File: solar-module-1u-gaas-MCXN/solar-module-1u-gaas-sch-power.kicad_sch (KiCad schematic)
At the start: 53 parts, among them Q1 NTR4101P, Q2 DMP2240UDM-7, U10 TPS63060DSCR, U12 LTC4412, U3 LT1618EMSTRPBF, U4 INA226

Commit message: Now solar module v1.2.
Upgraded CAN transciever to the 337, added version bits, removed silkscreen on cell outlines, double checked fastener heads, cleaned up documentation a lot, fixed ERCs and DRCs.
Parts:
- C12: DIS DIgiKey -> DigiKey; DPN 490-GRT21BC71E106KE13LCT-ND -> 490-GRT21BC71E106KE13KCT-ND; MPN GRT21BC71E106KE13L -> GRT21BC71E106KE13K
- C13, C20, C4: footprint oresat-passives:0603-C-NOSILK -> oresat-passives:0805-C-NOSILK; DIS DIgiKey -> DigiKey; DPN 490-12317-1-ND -> 490-GRT21BC71E106KE13KCT-ND; MPN GRT188R61C106KE13D -> GRT21BC71E106KE13K
- C15, C19, C23: footprint oresat-passives:0805-C-NOSILK -> oresat-passives:1206-C; DPN 490-9959-1-ND -> 490-12409-1-ND; MPN GRM21BR61E226ME44L -> GRT31CC81C226KE01L
- C18: DPN 587-4332-1-ND -> 490-GRT188C71C475KE13DCT-ND; MFR Taiyo Yuden -> Murata Electronics; MPN EMK107BBJ475KAHT -> GRT188C71C475KE13D
- C2: DIS DIgiKey -> DigiKey; DPN 399-14102-1-ND -> 399-12983-1-ND; MPN C0603C103J3GECAUTO -> C0603C103J5RACAUTO
- C21, C37, C6, C7, C8: DPN 587-3472-1-ND -> 399-6856-1-ND; MFR Taiyo Yuden -> KEMET; MPN TMK107BJ104KAHT -> C0603C104K5RACAUTO
- C22: DIS DIgiKey -> DigiKey; DPN 399-6840-1-ND -> 399-16015-1-ND; MPN C0603C100J5GACAUTO -> C0603C100J1GACAUTO
- Q1: DIS DIgiKey -> DigiKey; MFR On Semiconductor -> ON Semi
- Q2: DIS DIgiKey -> DigiKey
- U4: footprint Package_SO:VSSOP-10_3x3mm_P0.5mm -> Package_SO:TSSOP-10_3x3mm_P0.5mm
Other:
- moved on the sheet: C7

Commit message: Fixed Makefile to produce usable BOM. Updated BOM to correct DPNs, updated EOL'd components
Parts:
- D1, D3, L2, R18, R19, R2, R36, R37, R6, R7: DIS DIgiKey -> DigiKey
- D5: DIS DIgiKey -> DigiKey; DPN NRVB130LSFT1GOSTR-ND -> NRVB130LSFT1GOSCT-ND
- L1: DIS DIgiKey -> DigiKey; DPN 490-14160-2-ND -> 490-14160-1-ND
- Q1: DPN NTR4101PT1GOSCT-ND -> 31-DMP2035UQ-7CT-ND; MFR ON Semi -> Diodes Incorporated; MPN NTR4101PT1G -> DMP2035UQ-7
- R1: DIS DIgiKey -> DigiKey; DPN RMCF0603FT560KTR-ND -> RMCF0603FT560KCT-ND
- R10: DPN RMCF0603FT82K5TR-ND -> RMCF0603FT82K5CT-ND
- R12: DPN RMCF0603FT14K7TR-ND -> RMCF0603FT14K7CT-ND
- R16: DPN RMCF0603FT2K00TR-ND -> RMCF0603FT2K00CT-ND
- U10: DIS DIgiKey -> DigiKey; DPN 296-30204-2-ND -> 296-30204-1-ND
- U12: DIS DIgiKey -> DigiKey; DPN 505-LTC4412ES6#TRPBFTR-ND -> 505-LTC4412ES6#TRPBFCT-ND
- U3: DIS DIgiKey -> DigiKey; DPN LT1618EMS#TRPBFTR-ND -> LT1618EMS#TRPBFCT-ND
- U4: DIS DIgiKey -> DigiKey; DPN 296-29100-2-ND -> 296-29100-1-ND
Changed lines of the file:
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@@
 			)
 		)
-		(property "Datasheet" "https://www.onsemi.com/pdf/datasheet/ntr4101p-d.pdf"
+		(property "Datasheet" "https://www.diodes.com/assets/Datasheets/DMP2035U.pdf"
 			(at 307.34 95.25 0)
 			(hide yes)
@@
 			)
 		)
-		(property "Description" "P-Channel 20V 1.8A (Ta) 420mW (Ta) Surface Mount SOT-23-3 (TO-236)"
+		(property "Description" "P-Channel 20 V 4.9A (Ta) 810mW (Ta) Surface Mount SOT-23-3"
 			(at 307.34 95.25 0)
 			(hide yes)
@@
 			)
 		)
-		(property "DPN" "NTR4101PT1GOSCT-ND"
+		(property "DPN" "31-DMP2035UQ-7CT-ND"
 			(at 307.34 95.25 0)
 			(hide yes)
@@
 			)
 		)
-		(property "MFR" "ON Semi"
+		(property "MFR" "Diodes Incorporated"
 			(at 307.34 95.25 0)
 			(hide yes)
@@
 			)
 		)
-		(property "MPN" "NTR4101PT1G"
+		(property "MPN" "DMP2035UQ-7"
 			(at 307.34 95.25 0)
 			(hide yes)
@@
 			)
 		)
-		(property "DPN" "RMCF0603FT14K7TR-ND"
+		(property "DPN" "RMCF0603FT14K7CT-ND"
 			(at 234.95 83.82 0)
 			(hide yes)
@@
 			)
 		)
-		(property "DIS" "DIgiKey"
+		(property "DIS" "DigiKey"
 			(at 228.6 213.36 0)
 			(hide yes)
@@
 			)
 		)
-		(property "DIS" "DIgiKey"
+		(property "DIS" "DigiKey"
 			(at 191.77 208.28 0)
 			(hide yes)
@@
 			)
 		)
-		(property "DPN" "490-14160-2-ND"
+		(property "DPN" "490-14160-1-ND"
 			(at 191.77 208.28 0)
 			(hide yes)
@@
 			)
 		)
-		(property "DPN" "RMCF0603FT82K5TR-ND"
+		(property "DPN" "RMCF0603FT82K5CT-ND"
 			(at 234.95 69.85 0)
 			(hide yes)
@@
 			)
 		)
-		(property "DIS" "DIgiKey"
+		(property "DIS" "DigiKey"
 			(at 228.6 200.66 0)
 			(hide yes)
@@
 			)
 		)
-		(property "DPN" "RMCF0603FT560KTR-ND"
+		(property "DPN" "RMCF0603FT560KCT-ND"
 			(at 228.6 200.66 0)
 			(hide yes)
@@
 			)
 		)
-		(property "DIS" "DIgiKey"
+		(property "DIS" "DigiKey"
 			(at 210.82 62.23 0)
 			(hide yes)
@@
 			)
 		)
-		(property "DIS" "DIgiKey"
+		(property "DIS" "DigiKey"
 			(at 168.91 95.25 0)
 			(hide yes)
@@
 			)
 		)
-		(property "DIS" "DIgiKey"
+		(property "DIS" "DigiKey"
 			(at 204.47 203.2 0)
 			(hide yes)
@@
 			)
 		)
-		(property "DPN" "296-30204-2-ND"
+		(property "DPN" "296-30204-1-ND"
 			(at 204.47 203.2 0)
 			(hide yes)
@@
 			)
 		)
-		(property "DIS" "DIgiKey"
+		(property "DIS" "DigiKey"
 			(at 180.34 99.06 0)
 			(hide yes)
@@
 			)
 		)
-		(property "DIS" "DIgiKey"
+		(property "DIS" "DigiKey"
 			(at 81.28 71.12 0)
 			(hide yes)
@@
 			)
 		)
-		(property "DIS" "DIgiKey"
+		(property "DIS" "DigiKey"
 			(at 327.66 64.77 0)
 			(hide yes)
@@
 			)
 		)
-		(property "DPN" "505-LTC4412ES6#TRPBFTR-ND"
+		(property "DPN" "505-LTC4412ES6#TRPBFCT-ND"
 			(at 327.66 64.77 0)
 			(hide yes)
@@
 			)
 		)
-		(property "DIS" "DIgiKey"
+		(property "DIS" "DigiKey"
 			(at 299.72 88.9 0)
 			(hide yes)
@@
 			)
 		)
-		(property "DIS" "DIgiKey"
+		(property "DIS" "DigiKey"
 			(at 287.02 116.84 0)
 			(hide yes)
@@
 			)
 		)
-		(property "DIS" "DIgiKey"
+		(property "DIS" "DigiKey"
 			(at 226.06 62.23 0)
 			(hide yes)
@@
 			)
 		)
-		(property "DPN" "NRVB130LSFT1GOSTR-ND"
+		(property "DPN" "NRVB130LSFT1GOSCT-ND"
 			(at 226.06 62.23 0)
 			(hide yes)
@@
 			)
 		)
-		(property "DIS" "DIgiKey"
+		(property "DIS" "DigiKey"
 			(at 78.74 71.12 0)
 			(hide yes)
@@
 			)
 		)
-		(property "DPN" "RMCF0603FT2K00TR-ND"
+		(property "DPN" "RMCF0603FT2K00CT-ND"
 			(at 218.44 91.44 0)
 			(hide yes)
@@
 			)
 		)
-		(property "DIS" "DIgiKey"
+		(property "DIS" "DigiKey"
 			(at 287.02 130.81 0)
 			(hide yes)
@@
 			)
 		)
-		(property "DIS" "DIgiKey"
+		(property "DIS" "DigiKey"
 			(at 104.14 93.98 0)
 			(hide yes)
@@
 			)
 		)
-		(property "DPN" "296-29100-2-ND"
+		(property "DPN" "296-29100-1-ND"
 			(at 104.14 93.98 0)
 			(hide yes)
@@
 			)
 		)
-		(property "DIS" "DIgiKey"
+		(property "DIS" "DigiKey"
 			(at 198.12 86.36 0)
 			(hide yes)
@@
 			)
 		)
-		(property "DPN" "LT1618EMS#TRPBFTR-ND"
+		(property "DPN" "LT1618EMS#TRPBFCT-ND"
 			(at 198.12 86.36 0)
 			(hide yes)
@@
 			)
 		)
-		(property "DIS" "DIgiKey"
+		(property "DIS" "DigiKey"
 			(at 173.99 198.12 0)
 			(hide yes)

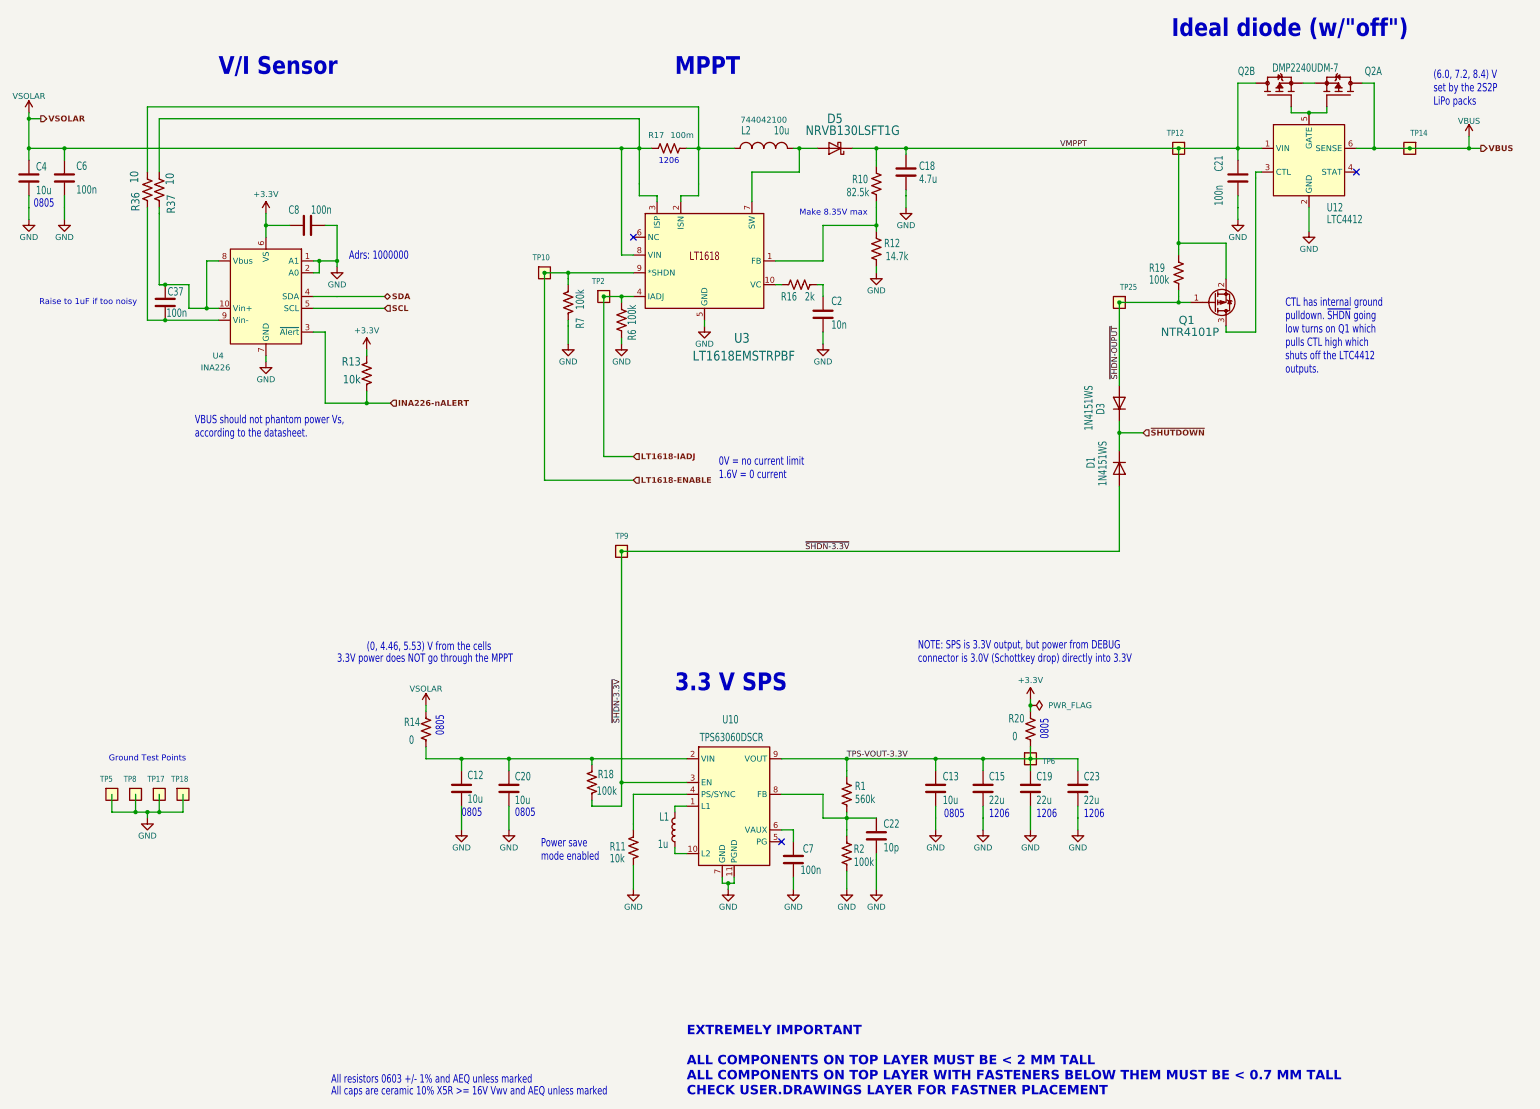
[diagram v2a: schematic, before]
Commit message: Minor polishing to schematic and board: fixed value font sizes and placement, imported value fixes to layout.
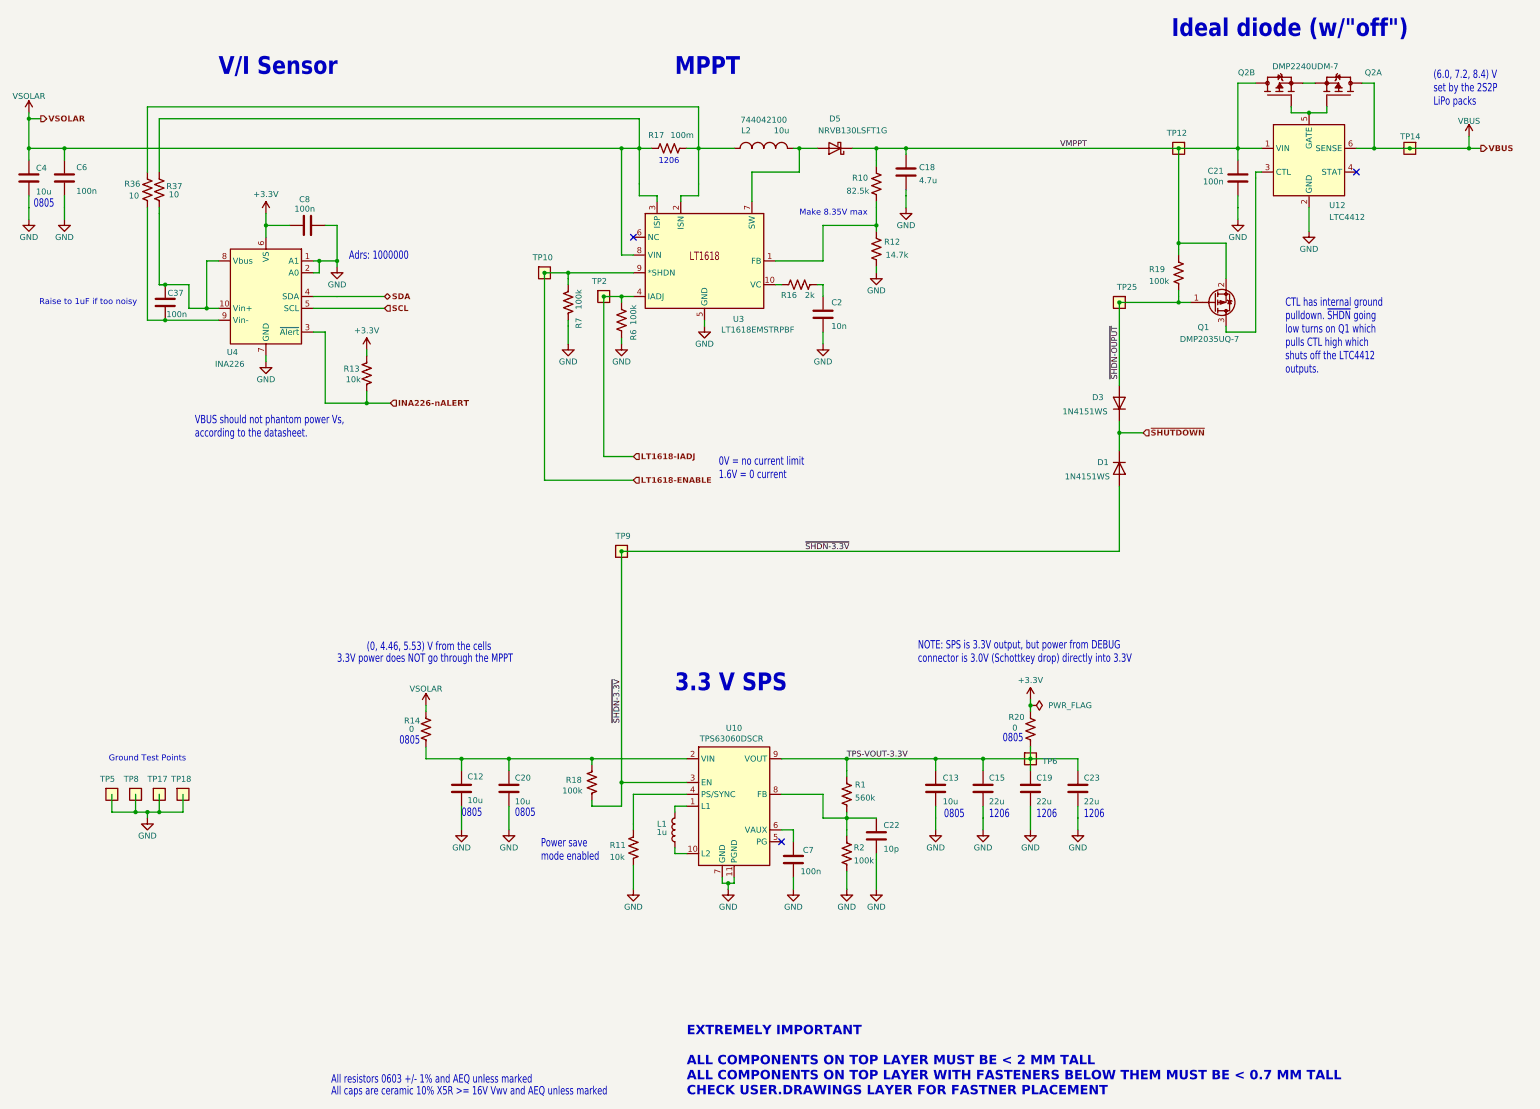
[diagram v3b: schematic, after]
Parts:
- Q1: value NTR4101P -> DMP2035UQ-7
